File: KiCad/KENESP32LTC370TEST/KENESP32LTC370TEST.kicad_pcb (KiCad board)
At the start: 2 copper layers, 47 parts, among them J1 Header Pins, Q1 BSC009NE2LS5IATMA1 A (TG2)(1A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, Q2 BSC009NE2LS5IATMA1 B (BG2)(1B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, Q3 BSC009NE2LS5IATMA1 C (BG1)(2A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, Q4 BSC009NE2LS5IATMA1 D (TG1)(2B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, U1 LTC3780EUH-TRPBF

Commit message: PCB Layout Continued
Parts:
- R26: footprint Resistor_SMD:R_1210_3225Metric_Pad1.30x2.65mm_HandSolder -> Resistor_SMD:R_1206_3216Metric_Pad1.30x1.75mm_HandSolder
- moved J1 199.7 mm to (107.1, 154.1), turned to 90 degrees
- moved D1 172.5 mm to (107.1, 142.0)
- moved C18 170.0 mm to (125.3, 143.8), turned to -90 degrees
- moved D3 170.0 mm to (110.5, 145.8), turned to 90 degrees
- moved R26 167.6 mm to (122.3, 149.6)
- moved C21 159.5 mm to (112.6, 142.1)
- moved C24 155.6 mm to (113.2, 145.9), turned to -90 degrees
- moved C23 153.0 mm to (118.3, 145.8), turned to 90 degrees
- moved C22 152.4 mm to (121.3, 145.8), turned to 90 degrees
- moved C14 146.9 mm to (108.0, 145.8), turned to 90 degrees
- moved C1 144.6 mm to (100.0, 124.3), turned to 90 degrees
- moved C3 143.7 mm to (97.5, 124.3), turned to 90 degrees
- moved C11 143.4 mm to (113.9, 138.3), turned to 90 degrees
- moved C12 141.5 mm to (110.1, 132.0), turned to 180 degrees
- moved C2 140.8 mm to (102.4, 124.3), turned to 90 degrees
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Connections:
- C1 pad 2: Net-(C1-Pad2) -> VIN
- C2 pad 2: Net-(C1-Pad2) -> VIN
- C3 pad 2: Net-(C1-Pad2) -> VIN
- D3 pad 1: VIN -> VCC
- R10 pad 2: GND -> (no net)
- R19 pad 2: GND -> (no net)
- R5 pad 1: Net-(C1-Pad2) -> VIN
- R5 pad 2: VIN -> VCC
- U1 pad 23: VIN -> VCC
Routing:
- net SHUNT+: track 0.00 -> 32.0 mm
- net (no net): track 0.00 -> 22.7 mm
- net SENSE-: track 0.00 -> 5.80 mm
- net SENSE+: track 0.00 -> 5.71 mm
- net TG2: vias 0 -> 1
- net TG1: vias 0 -> 1
- net BG2: vias 0 -> 1
- net BG1: vias 0 -> 1
- added copper zone on F.Cu, net SHUNT+
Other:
- board text added: "POWER GND"
- board text added: "SIGNAL GND"

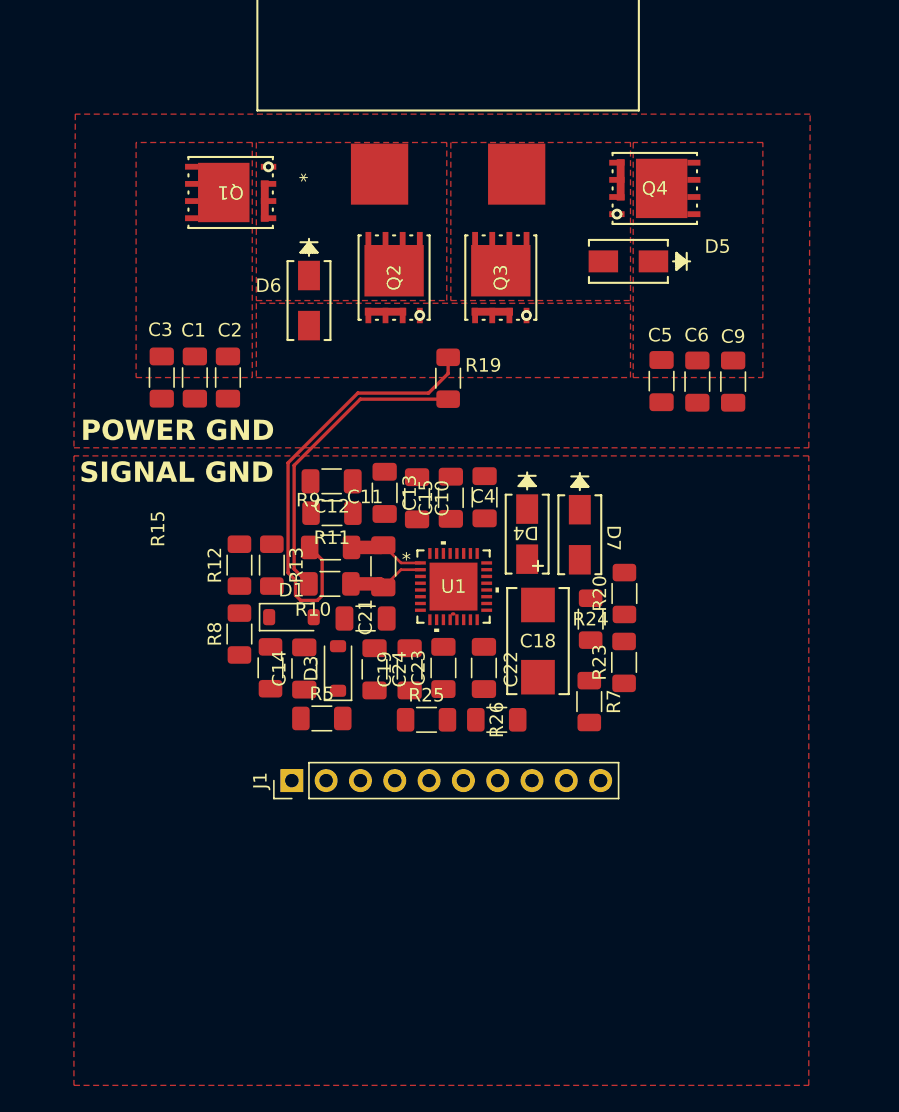
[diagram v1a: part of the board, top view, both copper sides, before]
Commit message: LTC3780 Completed. PCB Ordered
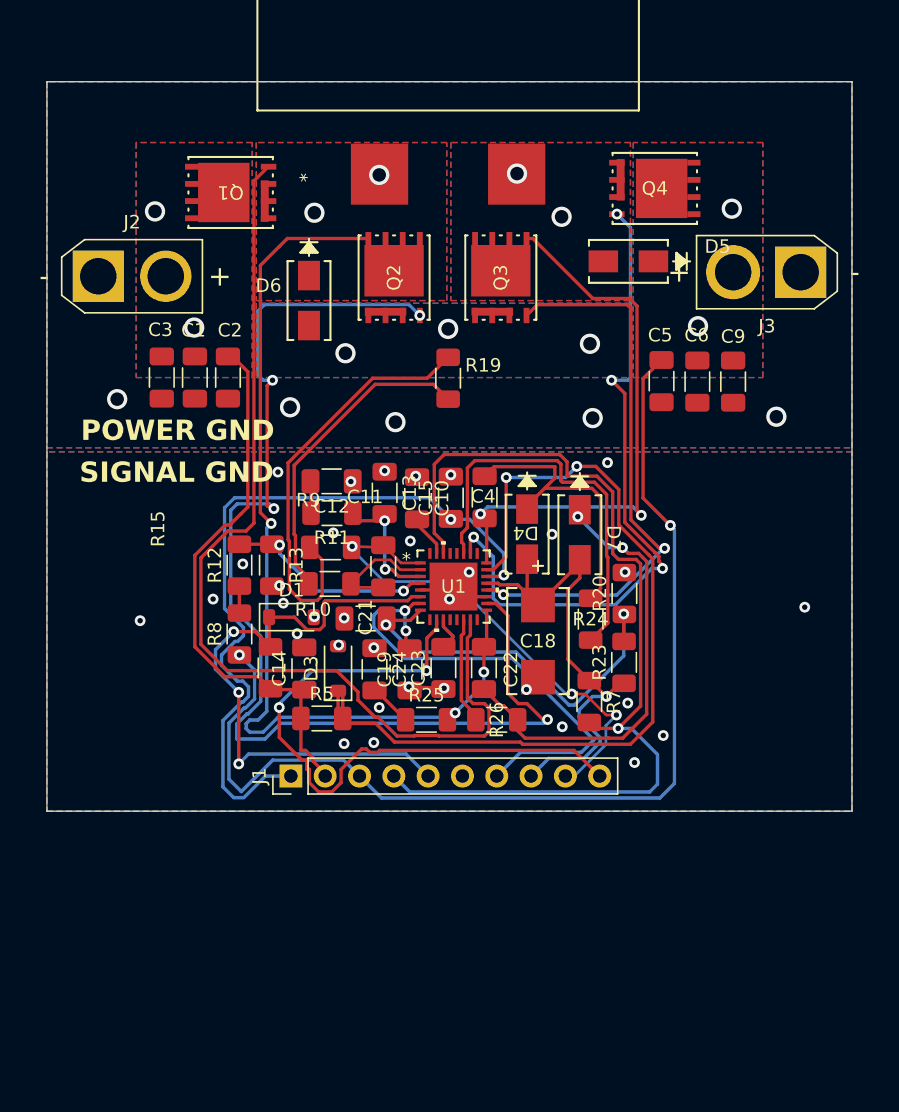
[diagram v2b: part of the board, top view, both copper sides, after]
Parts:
- added J2: Power In, Connector_AMASS:AMASS_XT30U-M_1x02_P5.0mm_Vertical, F.Cu at (92.8, 116.8)
- added J3: Power Out, Connector_AMASS:AMASS_XT30U-F_1x02_P5.0mm_Vertical, F.Cu at (144.8, 116.5)
- moved J1 0.34 mm to (107.1, 153.8)
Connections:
- R10 pad 2: (no net) -> GND
- R19 pad 2: (no net) -> GND
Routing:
- net BG2: track 0.00 -> 85.8 mm, vias 1 -> 4
- net VOUT: track 0.00 -> 79.3 mm, vias 0 -> 4
- net TG2: track 0.00 -> 72.4 mm, vias 1 -> 0
- net PGOOD: track 0.00 -> 70.4 mm, vias 0 -> 1
- net SW2: track 0.00 -> 69.3 mm, vias 0 -> 5
- net VCC: track 0.00 -> 64.3 mm, vias 0 -> 2
- net EXTVCC: track 0.00 -> 55.6 mm, vias 0 -> 2
- net TG1: track 0.00 -> 49.8 mm, vias 1 -> 4
- net PLLIN: track 0.00 -> 47.6 mm, vias 0 -> 2
- net RUN: track 0.00 -> 45.1 mm, vias 0 -> 3
- net SW1: track 0.00 -> 42.5 mm, vias 0 -> 4
- net BG1: track 0.00 -> 42.0 mm, vias 1 -> 2
- net VIN: track 0.00 -> 41.0 mm, vias 0 -> 2
- net INTVCC: track 0.09 -> 37.9 mm, vias 0 -> 1
- net FCB: track 0.00 -> 35.7 mm, vias 0 -> 2
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- added copper zone on B.Cu, net GND
- added copper zone on B.Cu, net SHUNT+
- added copper zone on B.Cu, net SW1
- added copper zone on B.Cu, net SW2
- added copper zone on B.Cu, net VIN
- added copper zone on B.Cu, net VOUT
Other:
- board outline added: 59.6 x 54 mm
